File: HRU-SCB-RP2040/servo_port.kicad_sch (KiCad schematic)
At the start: 32 parts, among them J1 Conn_01x03_Pin, J10 Conn_01x03_Pin, J11 Conn_01x03_Pin, J12 Conn_01x03_Pin, J13 Conn_01x03_Pin, J14 Conn_01x03_Pin, J15 Conn_01x03_Pin, J16 Conn_01x03_Pin, J17 Conn_01x03_Pin, J18 Conn_01x03_Pin, J19 Conn_01x03_Pin, J2 Conn_01x03_Pin, J20 Conn_01x03_Pin, J21 Conn_01x03_Pin, J22 Conn_01x03_Pin, J23 Conn_01x03_Pin, J24 Conn_01x03_Pin, J3 Conn_01x03_Pin, J4 Conn_01x03_Pin, J5 Conn_01x03_Pin, J6 Conn_01x03_Pin, J7 Conn_01x03_Pin, J8 Conn_01x03_Pin, J9 Conn_01x03_Pin, U2 PCA9685PW, U3 PCA9685PW

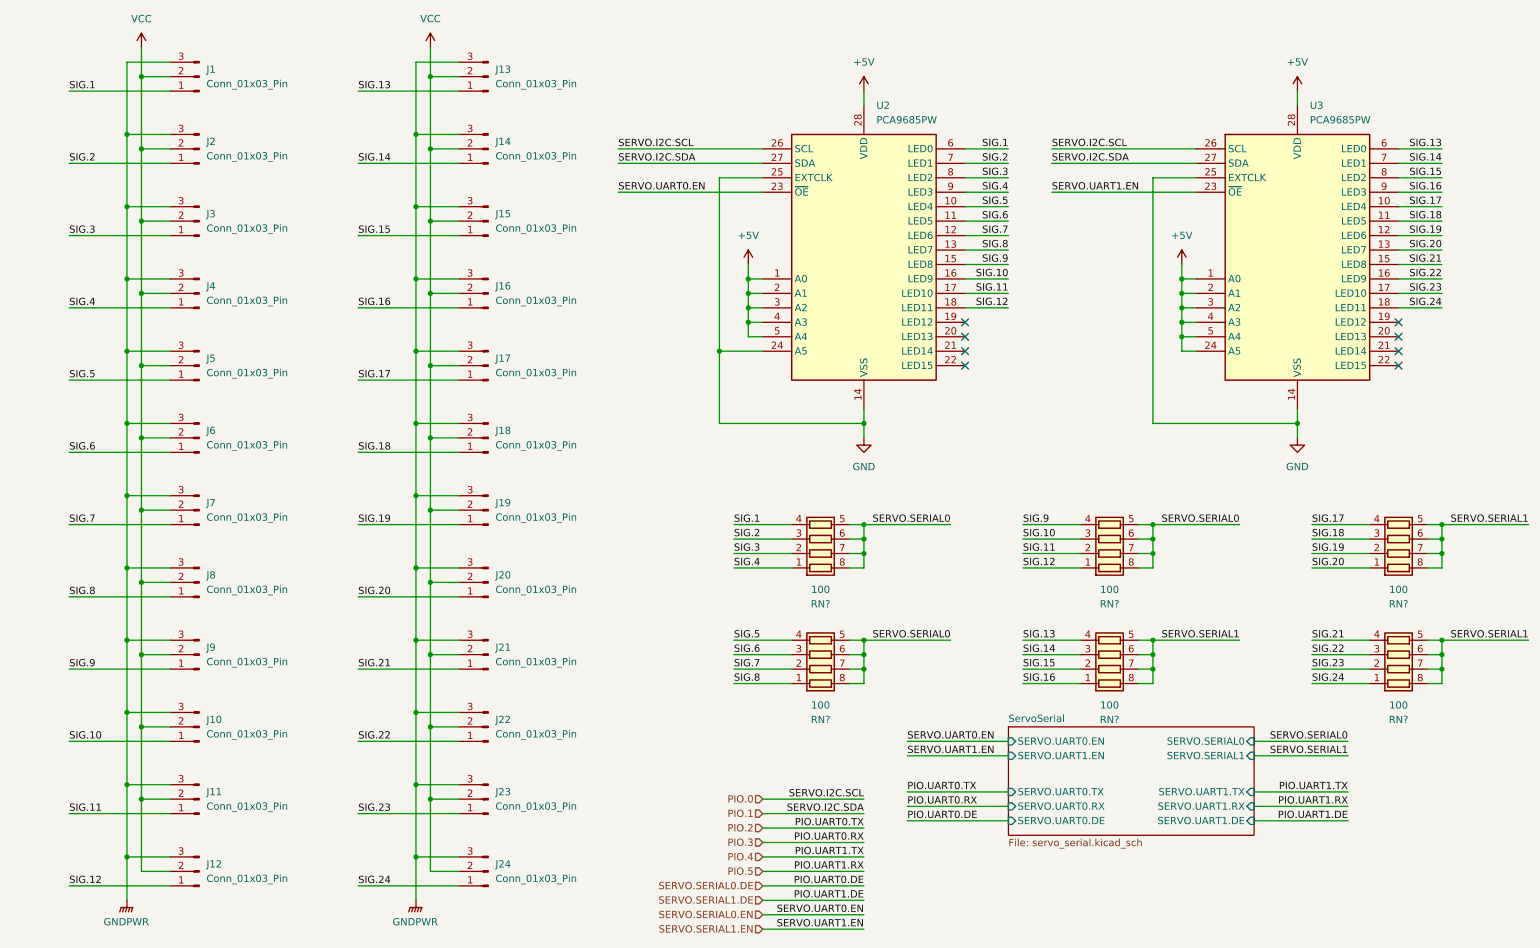
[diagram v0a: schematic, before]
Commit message: Delete PWM circuit
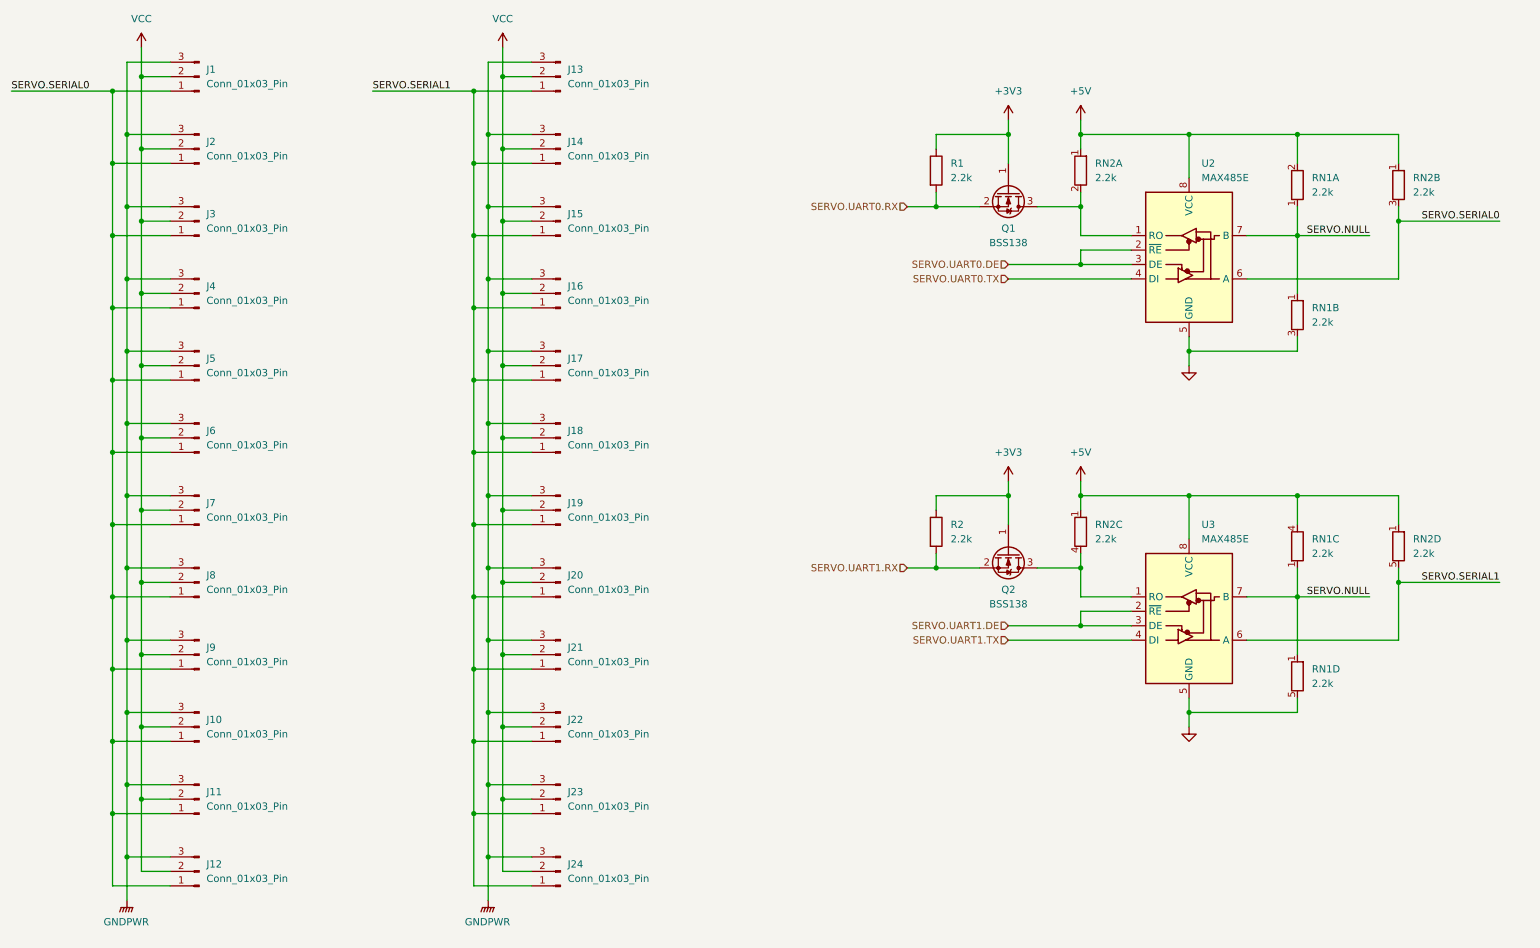
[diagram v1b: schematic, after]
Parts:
- removed RN? (x6): 100, Resistor_SMD:R_Array_Convex_4x1206, symbol Device:R_Pack04
- removed U2, U3: PCA9685PW, Package_SO:TSSOP-28_4.4x9.7mm_P0.65mm, symbol Driver_LED:PCA9685PW
- added Q1, Q2: BSS138, Package_TO_SOT_SMD:SOT-23, symbol Transistor_FET:BSS138
- added R1, R2: 2.2k, Resistor_THT:R_Axial_DIN0204_L3.6mm_D1.6mm_P5.08mm_Horizontal, symbol Device:R
- added RN1, RN2: 2.2k, Resistor_THT:R_Array_SIP5, symbol Device:R_Network04_Split
- added U2, U3: MAX485E, Package_SO:SOP-8_3.9x4.9mm_P1.27mm, symbol Interface_UART:MAX485E
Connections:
- net SIG.1 is gone; now on net SERVO.SERIAL0: J1.1 (Pin_1)
- net SIG.10 is gone; now on net SERVO.SERIAL0: J10.1 (Pin_1)
- net SIG.11 is gone; now on net SERVO.SERIAL0: J11.1 (Pin_1)
- net SIG.12 is gone; now on net SERVO.SERIAL0: J12.1 (Pin_1)
- net SIG.13 is gone; now on net SERVO.SERIAL1: J13.1 (Pin_1)
- net SIG.14 is gone; now on net SERVO.SERIAL1: J14.1 (Pin_1)
- net SIG.15 is gone; now on net SERVO.SERIAL1: J15.1 (Pin_1)
- net SIG.16 is gone; now on net SERVO.SERIAL1: J16.1 (Pin_1)
- net SIG.17 is gone; now on net SERVO.SERIAL1: J17.1 (Pin_1)
- net SIG.18 is gone; now on net SERVO.SERIAL1: J18.1 (Pin_1)
- net SIG.19 is gone; now on net SERVO.SERIAL1: J19.1 (Pin_1)
- net SIG.2 is gone; now on net SERVO.SERIAL0: J2.1 (Pin_1)
- net SIG.20 is gone; now on net SERVO.SERIAL1: J20.1 (Pin_1)
- net SIG.21 is gone; now on net SERVO.SERIAL1: J21.1 (Pin_1)
- net SIG.22 is gone; now on net SERVO.SERIAL1: J22.1 (Pin_1)
- net SIG.23 is gone; now on net SERVO.SERIAL1: J23.1 (Pin_1)
- net SIG.24 is gone; now on net SERVO.SERIAL1: J24.1 (Pin_1)
- net SIG.3 is gone; now on net SERVO.SERIAL0: J3.1 (Pin_1)
- net SIG.4 is gone; now on net SERVO.SERIAL0: J4.1 (Pin_1)
- net SIG.5 is gone; now on net SERVO.SERIAL0: J5.1 (Pin_1)
- net SIG.6 is gone; now on net SERVO.SERIAL0: J6.1 (Pin_1)
- net SIG.7 is gone; now on net SERVO.SERIAL0: J7.1 (Pin_1)
- net SIG.8 is gone; now on net SERVO.SERIAL0: J8.1 (Pin_1)
- net SIG.9 is gone; now on net SERVO.SERIAL0: J9.1 (Pin_1)
- net +5V: now also RN1.2 (R1.2), RN1.4 (R3.2), RN2.1 (R1), RN2.1 (R1), RN2.1 (R1), RN2.1 (R1), U2.8 (VCC), U3.8 (VCC)
- net GND: now also RN1.3 (R2.2), RN1.5 (R4.2), U2.5 (GND), U3.5 (GND)
- net SERVO.SERIAL0: now also RN2.3 (R2.2), U2.6 (A)
- net SERVO.SERIAL1: now also RN2.5 (R4.2), U3.6 (A)
- new net: Q1.3 (D), RN2.2 (R1.2), U2.1 (RO)
- new net: Q2.3 (D), RN2.4 (R3.2), U3.1 (RO)
- new net +3V3: Q1.1 (G), Q2.1 (G), R1.1, R2.1
- new net SERVO.NULL: RN1.1 (R1), RN1.1 (R1), RN1.1 (R1), RN1.1 (R1), U2.7 (B), U3.7 (B)
- new net SERVO.UART0.DE: U2.2 (~{RE}), U2.3 (DE)
- new net SERVO.UART0.RX: Q1.2 (S), R1.2
- new net SERVO.UART0.TX: U2.4 (DI)
- new net SERVO.UART1.DE: U3.2 (~{RE}), U3.3 (DE)
- new net SERVO.UART1.RX: Q2.2 (S), R2.2
- new net SERVO.UART1.TX: U3.4 (DI)
- no-connect marks 8 -> 0
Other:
- removed sheet ServoSerial

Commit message: Update design for hand soldering friendly
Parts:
- removed RN1, RN2: 2.2k, Resistor_THT:R_Array_SIP5, symbol Device:R_Network04_Split
- added R3, R4, R5, R6, R7, R8: 2.2k, Resistor_THT:R_Axial_DIN0204_L3.6mm_D1.6mm_P5.08mm_Horizontal, symbol Device:R
- Q1, Q2: value BSS138 -> NchFET; footprint Package_TO_SOT_SMD:SOT-23 -> Package_TO_SOT_THT:TO-92S
- U2, U3: footprint Package_SO:SOP-8_3.9x4.9mm_P1.27mm -> Package_DIP:DIP-8_W7.62mm_Socket
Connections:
- net +5V: now also R3.1, R4.1, R5.1, R7.1, R8.1
- net GND: now also R6.2
- net SERVO.NULL: now also R5.2, R6.1
- net SERVO.SERIAL0: now also R7.2
- net SERVO.SERIAL1: now also R8.2
- net at Q1.3 (D), U2.1 (RO): now also R3.2
- net at Q2.3 (D), U3.1 (RO): now also R4.2

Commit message: Update DCDC for DIP soldering
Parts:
- R1, R2, R4, R5, R6: value 2.2k -> 5.1k
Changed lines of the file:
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@@
 		(fields_autoplaced yes)
 		(property "Reference" "R1"
-			(at 180.34 43.18 0)
+			(at 180.34 43.1799 0)
 			(effects
 				(font
@@
 			)
 		)
-		(property "Value" "2.2k"
-			(at 180.34 45.72 0)
+		(property "Value" "5.1k"
+			(at 180.34 45.7199 0)
 			(effects
 				(font
@@
 		(fields_autoplaced yes)
 		(property "Reference" "R5"
-			(at 243.84 45.72 0)
+			(at 243.84 45.7199 0)
 			(effects
 				(font
@@
 			)
 		)
-		(property "Value" "2.2k"
-			(at 243.84 48.26 0)
+		(property "Value" "5.1k"
+			(at 243.84 48.2599 0)
 			(effects
 				(font
@@
 		(fields_autoplaced yes)
 		(property "Reference" "R2"
-			(at 180.34 106.68 0)
+			(at 180.34 106.6799 0)
 			(effects
 				(font
@@
 			)
 		)
-		(property "Value" "2.2k"
-			(at 180.34 109.22 0)
+		(property "Value" "5.1k"
+			(at 180.34 109.2199 0)
 			(effects
 				(font
@@
 		(fields_autoplaced yes)
 		(property "Reference" "R6"
-			(at 243.84 68.58 0)
+			(at 243.84 68.5799 0)
 			(effects
 				(font
@@
 			)
 		)
-		(property "Value" "2.2k"
-			(at 243.84 71.12 0)
+		(property "Value" "5.1k"
+			(at 243.84 71.1199 0)
 			(effects
 				(font
@@
 		(fields_autoplaced yes)
 		(property "Reference" "R4"
-			(at 205.74 106.68 0)
+			(at 205.74 106.6799 0)
 			(effects
 				(font
@@
 			)
 		)
-		(property "Value" "2.2k"
-			(at 205.74 109.22 0)
-			(effects
-				(font
+		(property "Value" "5.1k"
+			(at 205.74 109.2199 0)
+			(effects
+				(font

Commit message: Modify footprint of the registers and regulators
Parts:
- R1, R2, R3, R4, R5, R6, R7, R8: footprint Resistor_THT:R_Axial_DIN0204_L3.6mm_D1.6mm_P5.08mm_Horizontal -> Resistor_THT:R_Axial_DIN0207_L6.3mm_D2.5mm_P7.62mm_Horizontal
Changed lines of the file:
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@@
 			)
 		)
-		(property "Footprint" "Resistor_THT:R_Axial_DIN0204_L3.6mm_D1.6mm_P5.08mm_Horizontal"
+		(property "Footprint" "Resistor_THT:R_Axial_DIN0207_L6.3mm_D2.5mm_P7.62mm_Horizontal"
 			(at 176.022 44.45 90)
 			(effects
@@
 			)
 		)
-		(property "Footprint" "Resistor_THT:R_Axial_DIN0204_L3.6mm_D1.6mm_P5.08mm_Horizontal"
+		(property "Footprint" "Resistor_THT:R_Axial_DIN0207_L6.3mm_D2.5mm_P7.62mm_Horizontal"
 			(at 239.522 46.99 90)
 			(effects
@@
 			)
 		)
-		(property "Footprint" "Resistor_THT:R_Axial_DIN0204_L3.6mm_D1.6mm_P5.08mm_Horizontal"
+		(property "Footprint" "Resistor_THT:R_Axial_DIN0207_L6.3mm_D2.5mm_P7.62mm_Horizontal"
 			(at 257.302 46.99 90)
 			(effects
@@
 			)
 		)
-		(property "Footprint" "Resistor_THT:R_Axial_DIN0204_L3.6mm_D1.6mm_P5.08mm_Horizontal"
+		(property "Footprint" "Resistor_THT:R_Axial_DIN0207_L6.3mm_D2.5mm_P7.62mm_Horizontal"
 			(at 176.022 107.95 90)
 			(effects
@@
 			)
 		)
-		(property "Footprint" "Resistor_THT:R_Axial_DIN0204_L3.6mm_D1.6mm_P5.08mm_Horizontal"
+		(property "Footprint" "Resistor_THT:R_Axial_DIN0207_L6.3mm_D2.5mm_P7.62mm_Horizontal"
 			(at 257.302 110.49 90)
 			(effects
@@
 			)
 		)
-		(property "Footprint" "Resistor_THT:R_Axial_DIN0204_L3.6mm_D1.6mm_P5.08mm_Horizontal"
+		(property "Footprint" "Resistor_THT:R_Axial_DIN0207_L6.3mm_D2.5mm_P7.62mm_Horizontal"
 			(at 201.422 44.45 90)
 			(effects
@@
 			)
 		)
-		(property "Footprint" "Resistor_THT:R_Axial_DIN0204_L3.6mm_D1.6mm_P5.08mm_Horizontal"
+		(property "Footprint" "Resistor_THT:R_Axial_DIN0207_L6.3mm_D2.5mm_P7.62mm_Horizontal"
 			(at 239.522 69.85 90)
 			(effects
@@
 			)
 		)
-		(property "Footprint" "Resistor_THT:R_Axial_DIN0204_L3.6mm_D1.6mm_P5.08mm_Horizontal"
+		(property "Footprint" "Resistor_THT:R_Axial_DIN0207_L6.3mm_D2.5mm_P7.62mm_Horizontal"
 			(at 201.422 107.95 90)
 			(effects

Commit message: update: circuit design of HRU-SCB-RP2040
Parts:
- removed Q1, Q2: NchFET, Package_TO_SOT_THT:TO-92S, symbol Transistor_FET:BSS138
- added Q1, Q2: BS170, Package_TO_SOT_THT:TO-92_Inline_W4.0mm_Horizontal_FlatSideDown, symbol Transistor_FET:BS170
- R3: value 2.2k -> 5.1k
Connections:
- net +3V3: now also Q1.2 (G), Q2.2 (G)
- net SERVO.UART0.RX: now also Q1.3 (S)
- net SERVO.UART1.RX: now also Q2.3 (S)
- net at R4.2, U3.1 (RO): now also Q2.1 (D)
- net at R3.2, U2.1 (RO): now also Q1.1 (D)
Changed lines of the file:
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@@
 (kicad_sch
-	(version 20231120)
+	(version 20250114)
 	(generator "eeschema")
-	(generator_version "8.0")
+	(generator_version "9.0")
 	(paper "A4")
 	(junction
@@
 	(label "SERVO.NULL"
 		(at 254 55.88 180)
-		(fields_autoplaced yes)
 		(effects
 			(font
@@
 	(label "SERVO.SERIAL1"
 		(at 276.86 116.84 180)
-		(fields_autoplaced yes)
 		(effects
 			(font
@@
 	(label "SERVO.NULL"
 		(at 254 119.38 180)
-		(fields_autoplaced yes)
 		(effects
 			(font
@@
 	(label "SERVO.SERIAL0"
 		(at 15.24 30.48 0)
-		(fields_autoplaced yes)
 		(effects
 			(font
@@
 	(label "SERVO.SERIAL1"
 		(at 78.74 30.48 0)
-		(fields_autoplaced yes)
 		(effects
 			(font
@@
 	(label "SERVO.SERIAL0"
 		(at 276.86 53.34 180)
-		(fields_autoplaced yes)
 		(effects
 			(font
@@
 		(shape input)
 		(at 172.72 50.8 180)
-		(fields_autoplaced yes)
 		(effects
 			(font
@@
 		(shape input)
 		(at 190.5 63.5 180)
-		(fields_autoplaced yes)
 		(effects
 			(font
@@
 		(shape input)
 		(at 190.5 60.96 180)
-		(fields_autoplaced yes)
 		(effects
 			(font
@@
 		(shape input)
 		(at 190.5 127 180)
-		(fields_autoplaced yes)
 		(effects
 			(font
@@
 		(shape input)
 		(at 172.72 114.3 180)
-		(fields_autoplaced yes)
 		(effects
 			(font
@@
 		(shape input)
 		(at 190.5 124.46 180)
-		(fields_autoplaced yes)
 		(effects
 			(font
@@
 	(symbol
 		(lib_id "Device:R")
+		(at 203.2 44.45 0)
+		(unit 1)
+		(exclude_from_sim no)
+		(in_bom yes)
+		(on_board yes)
+		(dnp no)
+		(fields_autoplaced yes)
+		(property "Reference" "R3"
+			(at 205.74 43.1799 0)
+			(effects
+				(font
+					(size 1.27 1.27)
+				)
+				(justify left)
+			)
+		)
+		(property "Value" "5.1k"
+			(at 205.74 45.7199 0)
+			(effects
+				(font
+					(size 1.27 1.27)
+				)
+				(justify left)
+			)
+		)
+		(property "Footprint" "Resistor_THT:R_Axial_DIN0207_L6.3mm_D2.5mm_P7.62mm_Horizontal"
+			(at 201.422 44.45 90)
+			(effects
+				(font
+					(size 1.27 1.27)
+				)
+				(hide yes)
+			)
+		)
+		(property "Datasheet" "~"
+			(at 203.2 44.45 0)
+			(effects
+				(font
+					(size 1.27 1.27)
+				)
+				(hide yes)
+			)
+		)
+		(property "Description" ""
+			(at 203.2 44.45 0)
+			(effects
+				(font
+					(size 1.27 1.27)
+				)
+				(hide yes)
+			)
+		)
+		(pin "1"
+		)
+		(pin "2"
+		)
+		(instances
+			(project "HRU-SCB-RP2040"
+				(path "/22d57d1f-fa00-4148-a62a-8eb596ebbd21/0cbf7606-be01-4f49-97dc-43c83a99d446"
+					(reference "R3")
+					(unit 1)
+				)
+			)
+		)
+	)
+	(symbol
+		(lib_id "Device:R")
 		(at 177.8 44.45 0)
 		(unit 1)
@@
 	)
 	(symbol
-		(lib_id "Transistor_FET:BSS138")
-		(at 190.5 111.76 270)
-		(unit 1)
-		(exclude_from_sim no)
-		(in_bom yes)
-		(on_board yes)
-		(dnp no)
-		(fields_autoplaced yes)
-		(property "Reference" "Q2"
-			(at 190.5 118.11 90)
-			(effects
-				(font
-					(size 1.27 1.27)
-				)
-			)
-		)
-		(property "Value" "NchFET"
-			(at 190.5 120.65 90)
-			(effects
-				(font
-					(size 1.27 1.27)
-				)
-			)
-		)
-		(property "Footprint" "Package_TO_SOT_THT:TO-92S"
-			(at 188.595 116.84 0)
-			(effects
-				(font
-					(size 1.27 1.27)
-					(italic yes)
-				)
-				(justify left)
-				(hide yes)
-			)
-		)
-		(property "Datasheet" "https://www.onsemi.com/pub/Collateral/BSS138-D.PDF"
-			(at 190.5 111.76 0)
-			(effects
-				(font
-					(size 1.27 1.27)
-				)
-				(justify left)
-				(hide yes)
-			)
-		)
-		(property "Description" ""
-			(at 190.5 111.76 0)
-			(effects
-				(font
-					(size 1.27 1.27)
-				)
-				(hide yes)
-			)
-		)
-		(pin "1"
-		)
-		(pin "2"
-		)
-		(pin "3"
-		)
-		(instances
-			(project "HRU-SCB-RP2040"
-				(path "/22d57d1f-fa00-4148-a62a-8eb596ebbd21/0cbf7606-be01-4f49-97dc-43c83a99d446"
-					(reference "Q2")
-					(unit 1)
-				)
-			)
-		)
-	)
-	(symbol
 		(lib_id "Connector:Conn_01x03_Pin")
 		(at 111.76 53.34 180)
@@
 	)
 	(symbol
-		(lib_id "Connector:Conn_01x03_Pin")
-		(at 48.26 53.34 180)
+		(lib_id "Transistor_FET:BS170")
+		(at 190.5 48.26 270)
 		(unit 1)
 		(exclude_from_sim no)
@@
 		(dnp no)
 		(fields_autoplaced yes)
-		(property "Reference" "J3"
-			(at 49.53 52.07 0)
+		(property "Reference" "Q1"
+			(at 190.5 54.61 90)
 			(effects
 				(font
 					(size 1.27 1.27)
 				)
-				(justify right)
 			)
 		)
-		(property "Value" "Conn_01x03_Pin"
-			(at 49.53 54.61 0)
+		(property "Value" "BS170"
+			(at 190.5 57.15 90)
 			(effects
 				(font
 					(size 1.27 1.27)
 				)
-				(justify right)
 			)
 		)
-		(property "Footprint" "mymod:PinHeader_1x03_P2.54mm_Vertical_SmallCourtyard"
-			(at 48.26 53.34 0)
+		(property "Footprint" "Package_TO_SOT_THT:TO-92_Inline_W4.0mm_Horizontal_FlatSideDown"
+			(at 188.595 53.34 0)
 			(effects
 				(font
 					(size 1.27 1.27)
+					(italic yes)
 				)
+				(justify left)
 				(hide yes)
 			)
 		)
-		(property "Datasheet" "~"
-			(at 48.26 53.34 0)
+		(property "Datasheet" "https://www.onsemi.com/pub/Collateral/BS170-D.PDF"
+			(at 186.69 53.34 0)
 			(effects
 				(font
 					(size 1.27 1.27)
 				)
+				(justify left)
 				(hide yes)
 			)
 		)
-		(property "Description" ""
-			(at 48.26 53.34 0)
+		(property "Description" "0.5A Id, 60V Vds, N-Channel MOSFET, TO-92"
+			(at 190.5 48.26 0)
 			(effects
 				(font
@@
 			)
 		)
-		(pin "1"
-		)
 		(pin "2"
 		)
+		(pin "1"
+		)
 		(pin "3"
 		)
 		(instances
-			(project "HRU-SCB-RP2040"
+			(project ""
 				(path "/22d57d1f-fa00-4148-a62a-8eb596ebbd21/0cbf7606-be01-4f49-97dc-43c83a99d446"
-					(reference "J3")
+					(reference "Q1")
 					(unit 1)
 				)
@@
 	)
 	(symbol
-		(lib_id "Device:R")
-		(at 203.2 44.45 0)
+		(lib_id "Connector:Conn_01x03_Pin")
+		(at 48.26 53.34 180)
 		(unit 1)
 		(exclude_from_sim no)
@@
 		(dnp no)
 		(fields_autoplaced yes)
-		(property "Reference" "R3"
-			(at 205.74 43.18 0)
+		(property "Reference" "J3"
+			(at 49.53 52.07 0)
 			(effects
 				(font
 					(size 1.27 1.27)
 				)
-				(justify left)
+				(justify right)
 			)
 		)
-		(property "Value" "2.2k"
-			(at 205.74 45.72 0)
+		(property "Value" "Conn_01x03_Pin"
+			(at 49.53 54.61 0)
 			(effects
 				(font
 					(size 1.27 1.27)
 				)
-				(justify left)
+				(justify right)
 			)
 		)
-		(property "Footprint" "Resistor_THT:R_Axial_DIN0207_L6.3mm_D2.5mm_P7.62mm_Horizontal"
-			(at 201.422 44.45 90)
+		(property "Footprint" "mymod:PinHeader_1x03_P2.54mm_Vertical_SmallCourtyard"
+			(at 48.26 53.34 0)
 			(effects
 				(font
@@
 		)
 		(property "Datasheet" "~"
-			(at 203.2 44.45 0)
+			(at 48.26 53.34 0)
 			(effects
 				(font
@@
 		)
 		(property "Description" ""
-			(at 203.2 44.45 0)
+			(at 48.26 53.34 0)
 			(effects
 				(font
@@
 		(pin "2"
 		)
+		(pin "3"
+		)
 		(instances
 			(project "HRU-SCB-RP2040"
 				(path "/22d57d1f-fa00-4148-a62a-8eb596ebbd21/0cbf7606-be01-4f49-97dc-43c83a99d446"
-					(reference "R3")
+					(reference "J3")
 					(unit 1)
 				)
@@
 	)
 	(symbol
-		(lib_id "Transistor_FET:BSS138")
-		(at 190.5 48.26 270)
+		(lib_id "Transistor_FET:BS170")
+		(at 190.5 111.76 270)
 		(unit 1)
 		(exclude_from_sim no)
@@
 		(dnp no)
 		(fields_autoplaced yes)
-		(property "Reference" "Q1"
-			(at 190.5 54.61 90)
+		(property "Reference" "Q2"
+			(at 190.5 118.11 90)
 			(effects
 				(font
@@
 			)
 		)
-		(property "Value" "NchFET"
-			(at 190.5 57.15 90)
+		(property "Value" "BS170"
+			(at 190.5 120.65 90)
 			(effects
 				(font
@@
 			)
 		)
-		(property "Footprint" "Package_TO_SOT_THT:TO-92S"
-			(at 188.595 53.34 0)
+		(property "Footprint" "Package_TO_SOT_THT:TO-92_Inline_W4.0mm_Horizontal_FlatSideDown"
+			(at 188.595 116.84 0)
 			(effects
 				(font
@@
 			)
 		)
-		(property "Datasheet" "https://www.onsemi.com/pub/Collateral/BSS138-D.PDF"
-			(at 190.5 48.26 0)
+		(property "Datasheet" "https://www.onsemi.com/pub/Collateral/BS170-D.PDF"
+			(at 186.69 116.84 0)
 			(effects
 				(font
@@
 			)
 		)
-		(property "Description" ""
-			(at 190.5 48.26 0)
+		(property "Description" "0.5A Id, 60V Vds, N-Channel MOSFET, TO-92"
+			(at 190.5 111.76 0)
 			(effects
 				(font
@@
 			)
 		)
-		(pin "1"
-		)
 		(pin "2"
 		)
+		(pin "1"
+		)
 		(pin "3"
 		)
@@
 			(project "HRU-SCB-RP2040"
 				(path "/22d57d1f-fa00-4148-a62a-8eb596ebbd21/0cbf7606-be01-4f49-97dc-43c83a99d446"
-					(reference "Q1")
+					(reference "Q2")
 					(unit 1)
 				)
